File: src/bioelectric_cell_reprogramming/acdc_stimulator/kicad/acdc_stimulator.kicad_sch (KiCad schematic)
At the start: 32 parts, among them IC1 LTC3896EFE#PBF, J1 USB_C_Receptacle_USB2.0_14P, J2 Conn_01x02_Socket, J3 Conn_ARM_SWD_TagConnect_TC203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, SW1 SW_Push, SW2 SW_SPDT, U1 STM32G431CBU3, U2 USBLC6-2SC6, U3 AMS1117-3.3, Y1 16Mhz

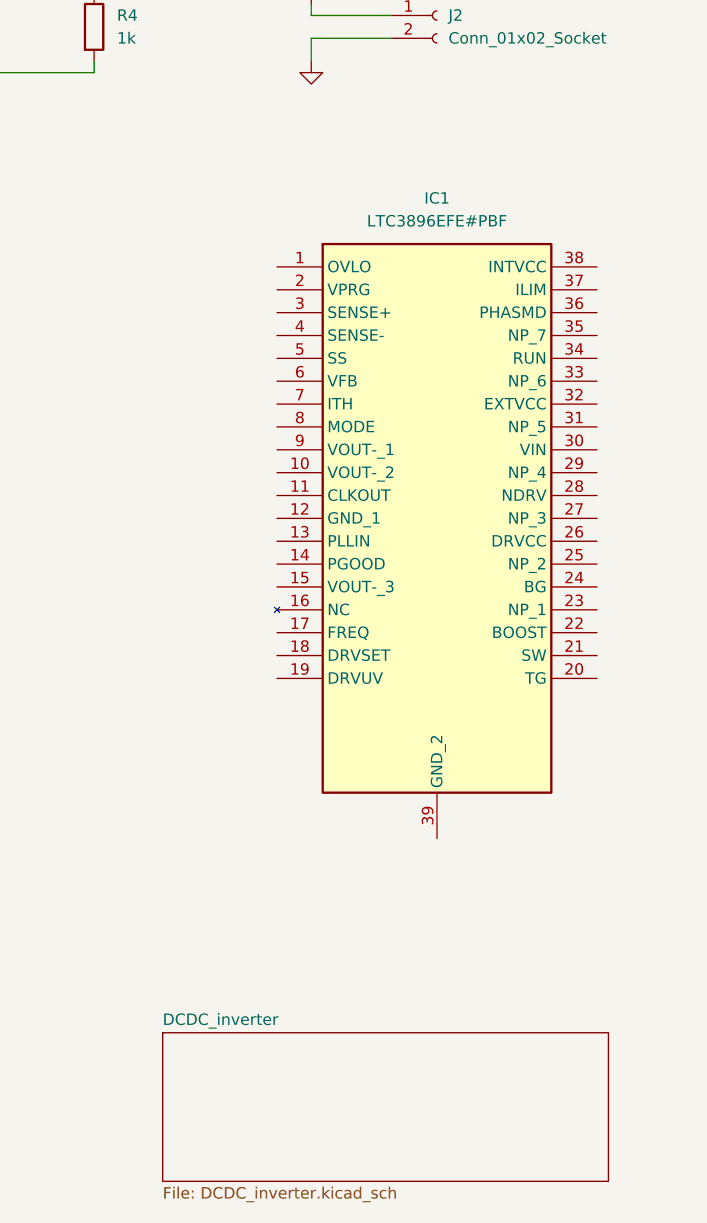
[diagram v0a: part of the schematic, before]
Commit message: finished schematic for DC/DC inverter
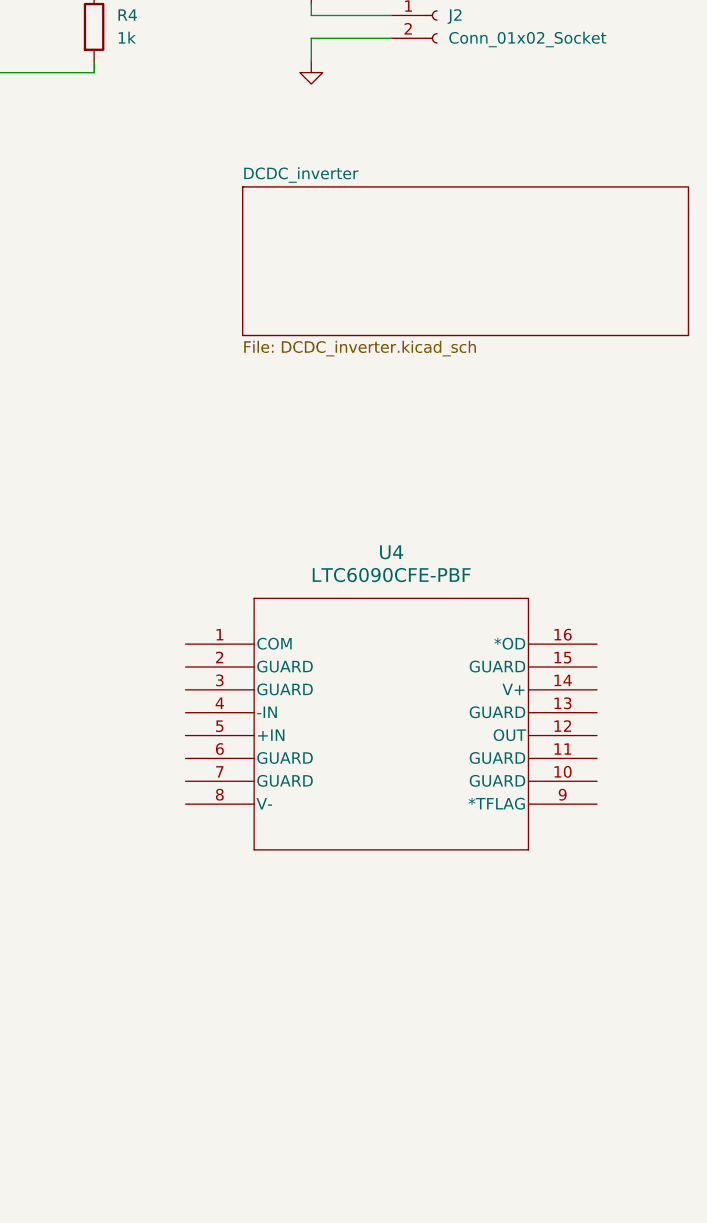
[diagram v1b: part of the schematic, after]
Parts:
- removed IC1: LTC3896EFE#PBF, SOP50P640X120-39N, symbol LTC3896EFE#PBF:LTC3896EFE#PBF
- added U4: LTC6090CFE-PBF, TSSOP-16_FE/BA_LIT, symbol LTC6090CFE_PBF:LTC6090CFE-PBF
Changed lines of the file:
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@@
-	)
-	(symbol
-		(lib_id "LTC3896EFE#PBF:LTC3896EFE#PBF")
-		(at 228.6 55.88 0)
-		(unit 1)
-		(exclude_from_sim no)
-		(in_bom yes)
-		(on_board yes)
-		(dnp no)
-		(fields_autoplaced yes)
-		(property "Reference" "IC1"
-			(at 246.38 48.26 0)
-			(effects
-				(font
-					(size 1.27 1.27)
-				)
-			)
-		)
-		(property "Value" "LTC3896EFE#PBF"
-			(at 246.38 50.8 0)
-			(effects
-				(font
-					(size 1.27 1.27)
-				)
-			)
-		)
-		(property "Footprint" "SOP50P640X120-39N"
-			(at 260.35 150.8 0)
-			(effects
-				(font
-					(size 1.27 1.27)
-				)
-				(justify left top)
-				(hide yes)
-			)
-		)
-		(property "Datasheet" "https://www.analog.com/media/en/technical-documentation/data-sheets/3896f.pdf"
-			(at 260.35 250.8 0)
-			(effects
-				(font
-					(size 1.27 1.27)
-				)
-				(justify left top)
-				(hide yes)
-			)
-		)
-		(property "Description" "LINEAR TECHNOLOGY - LTC3896EFE#PBF - DC/DC CTRL, INVERTING, 900KHZ, TSSOP-38"
-			(at 228.6 55.88 0)
-			(effects
-				(font
-					(size 1.27 1.27)
-				)
-				(hide yes)
-			)
-		)
-		(property "Height" "1.2"
-			(at 260.35 450.8 0)
-			(effects
-				(font
-					(size 1.27 1.27)
-				)
-				(justify left top)
-				(hide yes)
-			)
-		)
-		(property "Manufacturer_Name" "Analog Devices"
-			(at 260.35 550.8 0)
-			(effects
-				(font
-					(size 1.27 1.27)
-				)
-				(justify left top)
-				(hide yes)
-			)
-		)
-		(property "Manufacturer_Part_Number" "LTC3896EFE#PBF"
-			(at 260.35 650.8 0)
-			(effects
-				(font
-					(size 1.27 1.27)
-				)
-				(justify left top)
-				(hide yes)
-			)
-		)
-		(property "Mouser Part Number" "584-LTC3896EFE#PBF"
-			(at 260.35 750.8 0)
-			(effects
-				(font
-					(size 1.27 1.27)
-				)
-				(justify left top)
-				(hide yes)
-			)
-		)
-		(property "Mouser Price/Stock" "https://www.mouser.co.uk/ProductDetail/Analog-Devices/LTC3896EFEPBF?qs=oahfZPh6IAIYB3Kp6X%252BPyQ%3D%3D"
-			(at 260.35 850.8 0)
-			(effects
-				(font
-					(size 1.27 1.27)
-				)
-				(justify left top)
-				(hide yes)
-			)
-		)
-		(property "Arrow Part Number" "LTC3896EFE#PBF"
-			(at 260.35 950.8 0)
-			(effects
-				(font
-					(size 1.27 1.27)
-				)
-				(justify left top)
-				(hide yes)
-			)
-		)
-		(property "Arrow Price/Stock" "https://www.arrow.com/en/products/ltc3896efepbf/analog-devices?region=nac"
-			(at 260.35 1050.8 0)
-			(effects
-				(font
-					(size 1.27 1.27)
-				)
-				(justify left top)
-				(hide yes)
-			)
-		)
-		(pin "38"
-		)
-		(pin "11"
-		)
-		(pin "6"
-		)
-		(pin "8"
-		)
-		(pin "14"
-		)
-		(pin "37"
-		)
-		(pin "9"
-		)
-		(pin "35"
-		)
-		(pin "34"
-		)
-		(pin "22"
-		)
-		(pin "23"
-		)
-		(pin "24"
-		)
-		(pin "21"
-		)
-		(pin "15"
-		)
-		(pin "31"
-		)
-		(pin "27"
-		)
-		(pin "30"
-		)
-		(pin "10"
-		)
-		(pin "39"
-		)
-		(pin "29"
-		)
-		(pin "18"
-		)
-		(pin "3"
-		)
-		(pin "36"
-		)
-		(pin "25"
-		)
-		(pin "26"
-		)
-		(pin "1"
-		)
-		(pin "33"
-		)
-		(pin "17"
-		)
-		(pin "32"
-		)
-		(pin "16"
-		)
-		(pin "4"
-		)
-		(pin "13"
-		)
-		(pin "20"
-		)
-		(pin "5"
-		)
-		(pin "12"
-		)
-		(pin "28"
-		)
-		(pin "7"
-		)
-		(pin "2"
-		)
-		(pin "19"
-		)
-		(instances
-			(project ""
-				(path "/ec70e9f6-566f-44ea-8141-5580f51beca4"
-					(reference "IC1")
-					(unit 1)
-				)
-			)
-		)
 	)
 	(symbol
@@
 	)
 	(symbol
+		(lib_id "LTC6090CFE_PBF:LTC6090CFE-PBF")
+		(at 218.44 97.79 0)
+		(unit 1)
+		(exclude_from_sim no)
+		(in_bom yes)
+		(on_board yes)
+		(dnp no)
+		(fields_autoplaced yes)
+		(property "Reference" "U4"
+			(at 241.3 87.63 0)
+			(effects
+				(font
+					(size 1.524 1.524)
+				)
+			)
+		)
+		(property "Value" "LTC6090CFE-PBF"
+			(at 241.3 90.17 0)
+			(effects
+				(font
+					(size 1.524 1.524)
+				)
+			)
+		)
+		(property "Footprint" "TSSOP-16_FE/BA_LIT"
+			(at 218.44 97.79 0)
+			(effects
+				(font
+					(size 1.27 1.27)
+					(italic yes)
+				)
+				(hide yes)
+			)
+		)
+		(property "Datasheet" "LTC6090CFE-PBF"
+			(at 218.44 97.79 0)
+			(effects
+				(font
+					(size 1.27 1.27)
+					(italic yes)
+				)
+				(hide yes)
+			)
+		)
+		(property "Description" ""
+			(at 218.44 97.79 0)
+			(effects
+				(font
+					(size 1.27 1.27)
+				)
+				(hide yes)
+			)
+		)
+		(pin "15"
+		)
+		(pin "12"
+		)
+		(pin "2"
+		)
+		(pin "9"
+		)
+		(pin "11"
+		)
+		(pin "8"
+		)
+		(pin "16"
+		)
+		(pin "4"
+		)
+		(pin "3"
+		)
+		(pin "6"
+		)
+		(pin "5"
+		)
+		(pin "14"
+		)
+		(pin "13"
+		)
+		(pin "1"
+		)
+		(pin "10"
+		)
+		(pin "7"
+		)
+		(instances
+			(project ""
+				(path "/ec70e9f6-566f-44ea-8141-5580f51beca4"
+					(reference "U4")
+					(unit 1)
+				)
+			)
+		)
+	)
+	(symbol
 		(lib_id "Device:C")
 		(at 86.36 29.21 0)
@@
 	)
 	(sheet
-		(at 215.9 140.97)
+		(at 224.79 46.99)
 		(size 49.53 16.51)
 		(fields_autoplaced yes)
@@
 		)
 		(property "Sheetname" "DCDC_inverter"
-			(at 215.9 140.2584 0)
+			(at 224.79 46.2784 0)
 			(effects
 				(font
@@
 		)
 		(property "Sheetfile" "DCDC_inverter.kicad_sch"
-			(at 215.9 158.0646 0)
+			(at 224.79 64.0846 0)
 			(effects
 				(font
@@
 		)
 		(instances
-			(project "AC_EF"
+			(project "acdc_stimulator"
 				(path "/ec70e9f6-566f-44ea-8141-5580f51beca4"
 					(page "2")

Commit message: ci: main AC/DC schematic done minus incubator peripherals
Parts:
- removed U4: LTC6090CFE-PBF, TSSOP-16_FE/BA_LIT, symbol LTC6090CFE_PBF:LTC6090CFE-PBF
- added C37: 10n, symbol Device:C
- added C38, C40: 100n, symbol Device:C
- added C39: 10uF, symbol Device:C_Polarized
- added C41: 0.1u, symbol Device:C
- added C42: 10u, symbol Device:C
- added C43: 0, symbol Device:C
- added IC1: AD9833BRM-REEL7, SOP50P490X110-10N, symbol AD9833BRM-REEL7:AD9833BRM-REEL7
- added IC3: AD5122BCPZ10-RL7, QFN50P300X300X80-17N-D, symbol AD5122BCPZ10-RL7:AD5122BCPZ10-RL7
- added J4: Screw_Terminal_01x02, symbol Connector:Screw_Terminal_01x02
- added L2, L3: 0, symbol Device:L
- added Q10: BSZ096N10LS5ATMA1, BSZ060NE2LS, symbol BSZ096N10LS5ATMA1:BSZ096N10LS5ATMA1
- added R11, R18, R19: 10k, symbol Device:R
- added R12: 172k, symbol Device:R
- added R15, R16, R17: 0, symbol Device:R
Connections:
- net +3.3V: now also C41.1, C42.1, IC3.9 (VDD)
- net +5V: now also C37.1, C38.2, C39.1, IC1.2 (VDD)
- net GND: now also C38.1, C39.2, C40.1, C41.2, C42.2, IC1.4 (DGND), IC1.9 (AGND), IC3.1 (GND), IC3.17 (EP), IC3.4 (B1), IC3.5 (VSS), R11.1, R19.2
- net HSE_OUT: now also IC1.5 (MCLK)
- net DAC_DC: now reaches U1.12 (PA4)
- net DAC_AC: now reaches U1.13 (PA5)
- net DAC_AC: now also R18.1
- net H_Bridge_IN1: now reaches U1.25 (PB12)
- net H_Bridge_IN1: now also R15.1
- net H_Bridge_IN2: now reaches U1.26 (PB13)
- net H_Bridge_IN2: now also R16.1
- net VAC_ON: now reaches U1.29 (PC6)
- net VAC_ON: now also Q10.4 (G)
- net FG_CS: now reaches U1.30 (PA8)
- net FG_CS: now also IC1.8 (FSYNC)
- net POT_CS: now reaches U1.31 (PA9)
- net POT_CS: now also IC3.14 (~{SYNC})
- net SCLK: now reaches U1.39 (PC10)
- net SCLK: now also IC1.7 (SCLK), IC3.11 (SCLK)
- net SDI: now reaches U1.40 (PC11)
- net SDI: now also IC3.12 (SDI)
- net SDO: now reaches U1.43 (PB5)
- net SDO: now also IC1.6 (SDATA), IC3.13 (SDO)
- new net: IC3.10 (VLOGIC), IC3.16 (~{RESET})
- new net: C37.2, IC1.1 (COMP)
- new net: C40.2, IC1.3 (CAP/2.5V)
- new net: J4.1 (Pin_1), L2.2
- new net: C43.1, J4.2 (Pin_2), L3.2
- new net FG_OUT: IC1.10 (VOUT), IC3.2 (A1)
- new net H_Bridge/IN1: R15.2
- new net H_Bridge/IN2: R16.2
- new net LTC6090_AC/+IN: R18.2, R19.1
- new net LTC6090_AC/OUT: Q10.5 (D_1), Q10.6 (D_2), Q10.7 (D_3), Q10.8 (D_4), R17.2
- new net LTC6090_DC/-IN: R11.2, R12.1
- new net POT_OUT: IC3.3 (W1), R17.1
- new net VAC: C43.2, Q10.1 (S_1), Q10.2 (S_2), Q10.3 (S_3)
- new net VDC1: L2.1
- new net VDC2: L3.1
- new net V_DC: R12.2
- no-connect marks 0 -> 4
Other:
- added sheet H_Bridge (H_Bridge.kicad_sch)
- added sheet LTC6090_AC (LTC6090_AC.kicad_sch)
- added sheet LTC6090_DC (LTC6090_DC.kicad_sch)
- moved on the sheet: J2

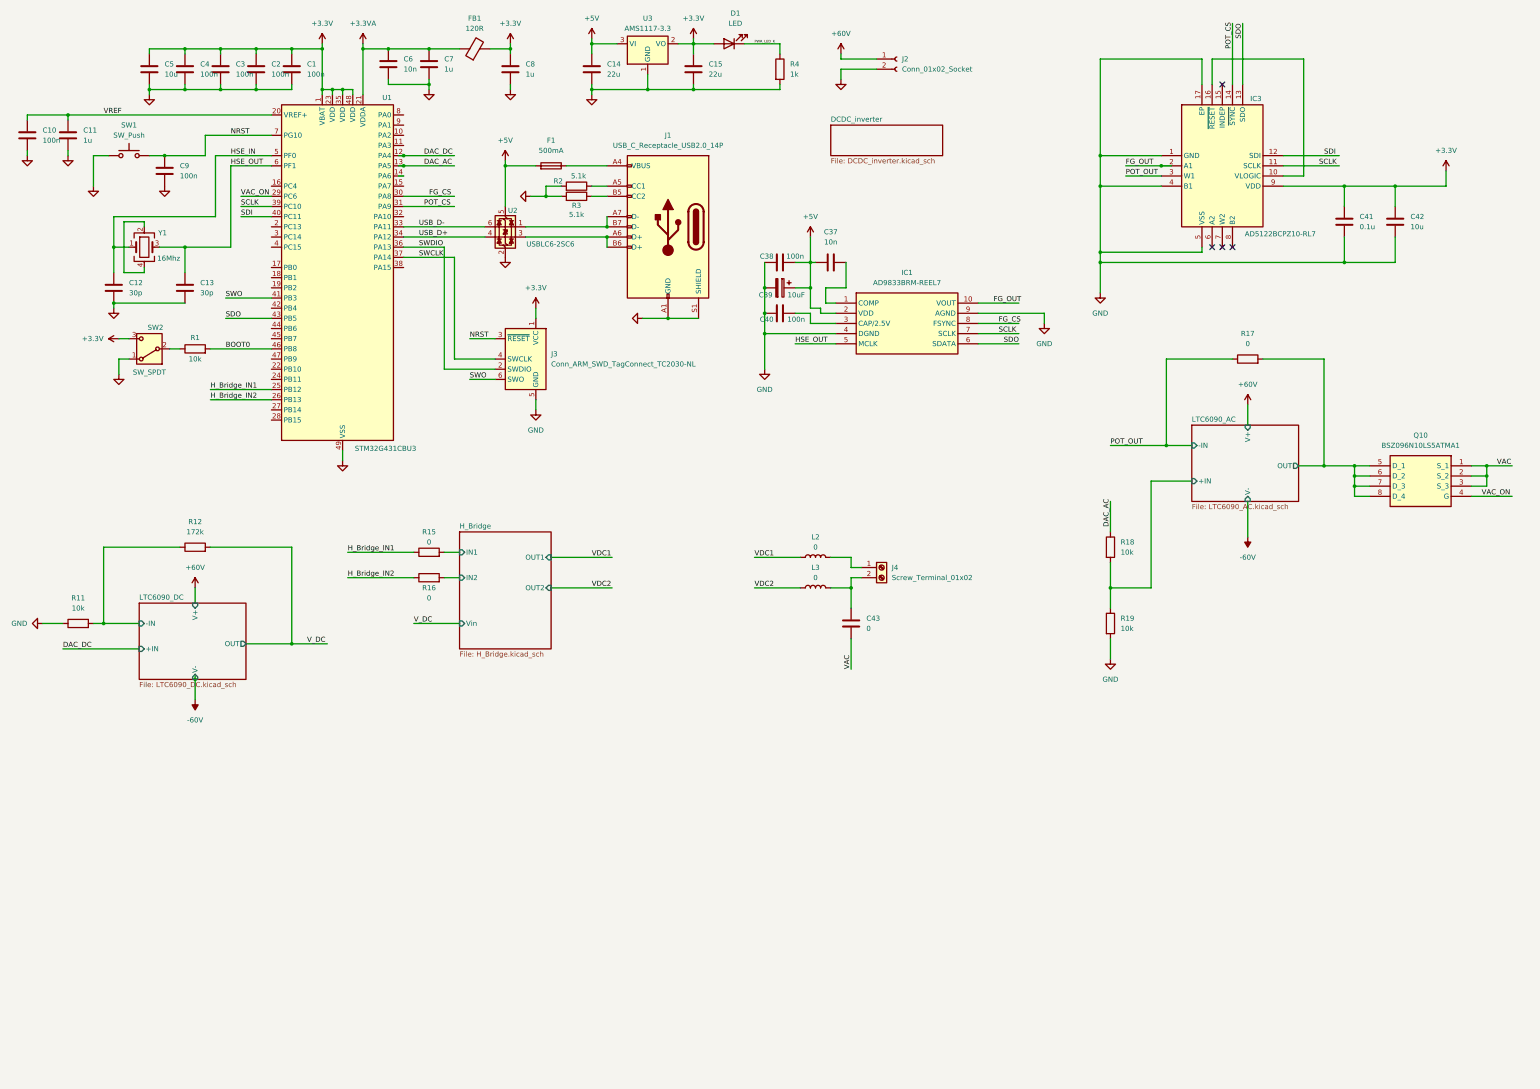
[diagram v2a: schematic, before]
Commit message: fix: added new STM32 with 3 DAC output pins
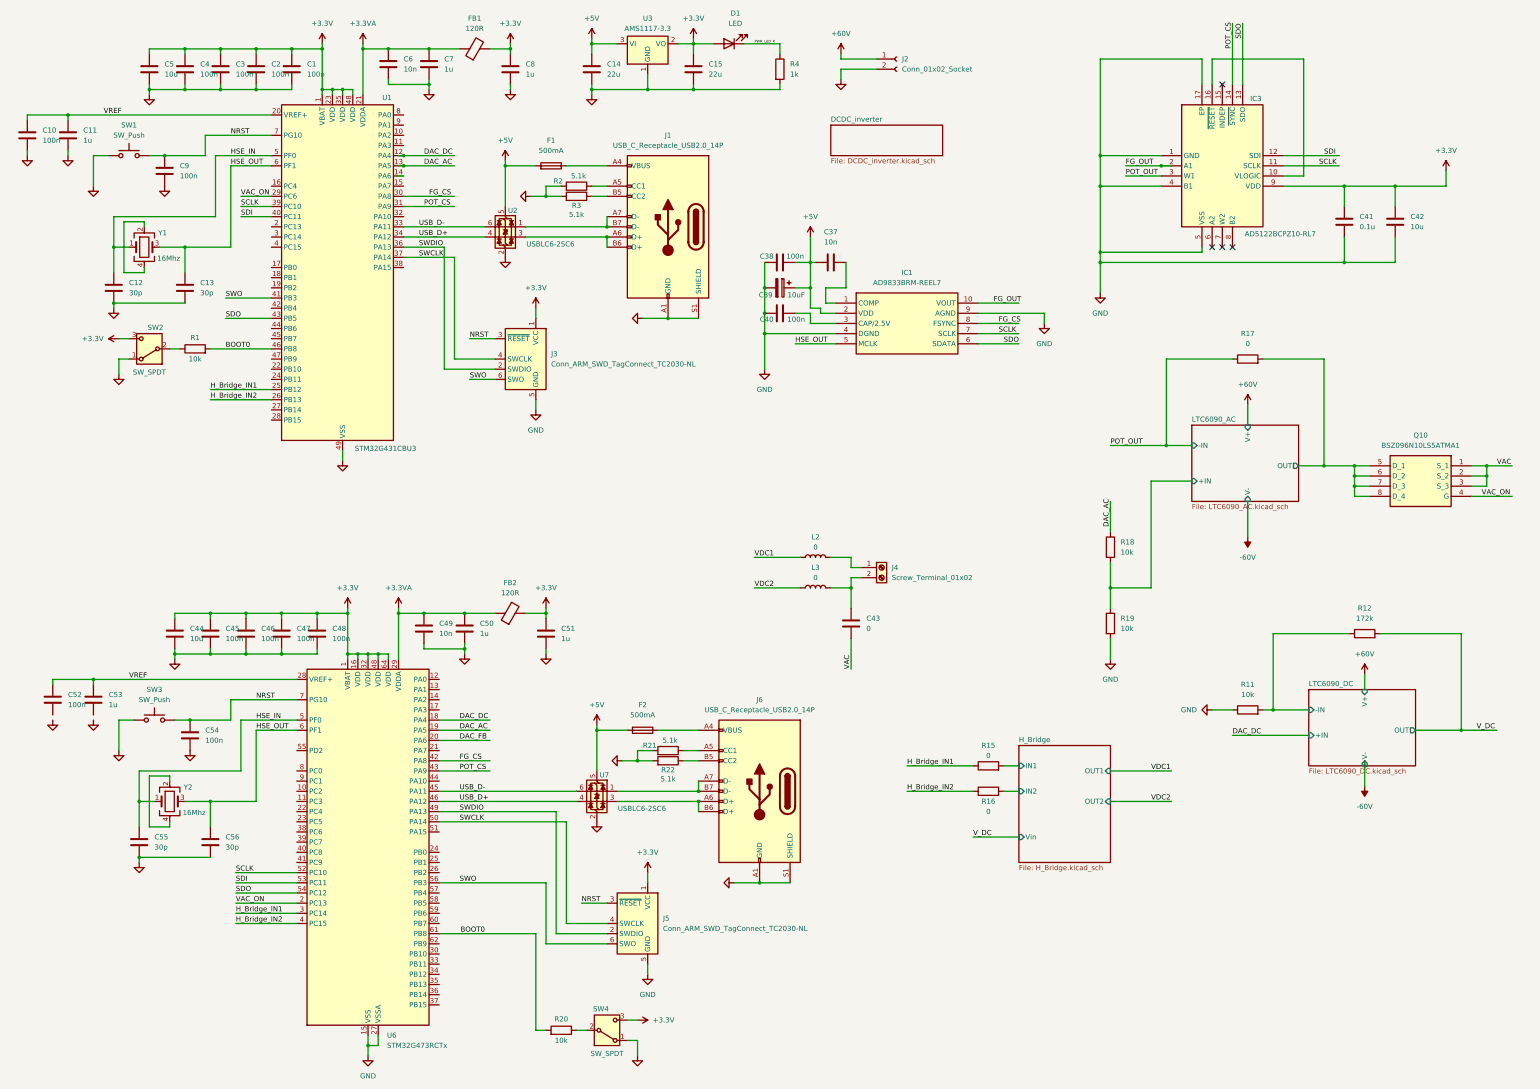
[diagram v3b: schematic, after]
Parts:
- added C44: 10u, symbol Device:C
- added C45, C46, C47, C48: 100n, symbol Device:C
- added C49: 10n, symbol Device:C
- added C50, C51: 1u, symbol Device:C
- added C52, C54: 100n, Capacitor_SMD:C_0402_1005Metric, symbol Device:C
- added C53: 1u, Capacitor_SMD:C_0402_1005Metric, symbol Device:C
- added C55, C56: 30p, symbol Device:C
- added F2: 500mA, Fuse:Fuse_0603_1608Metric, symbol Device:Fuse
- added FB2: 120R, symbol Device:FerriteBead
- added J5: Conn_ARM_SWD_TagConnect_TC2030-NL, Connector:Tag-Connect_TC2030-IDC-NL_2x03_P1.27mm_Vertical, symbol Connector:Conn_ARM_SWD_TagConnect_TC2030-NL
- added J6: USB_C_Receptacle_USB2.0_14P, Connector_USB:USB_C_Receptacle_GCT_USB4105-xx-A_16P_TopMnt_Horizontal, symbol Connector:USB_C_Receptacle_USB2.0_14P
- added R20: 10k, symbol Device:R
- added R21, R22: 5.1k, Resistor_SMD:R_0603_1608Metric, symbol Device:R
- added SW3: SW_Push, Button_Switch_THT:SW_PUSH-12mm_Wuerth-430476085716, symbol Switch:SW_Push
- added SW4: SW_SPDT, symbol Switch:SW_SPDT
- added U6: STM32G473RCTx, Package_QFP:LQFP-64_10x10mm_P0.5mm, symbol MCU_ST_STM32G4:STM32G473RCTx
- added U7: USBLC6-2SC6, Package_TO_SOT_SMD:SOT-23-6, symbol Power_Protection:USBLC6-2SC6
- added Y2: 16Mhz, symbol Device:Crystal_GND24
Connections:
- net +3.3V: now also C44.1, C45.1, C46.1, C47.1, C48.1, C51.1, FB2.2, J5.1 (VCC), SW4.3 (C), U6.1 (VBAT), U6.16 (VDD), U6.32 (VDD), U6.48 (VDD), U6.64 (VDD)
- net +3.3VA: now also C49.1, C50.1, FB2.1, U6.29 (VDDA)
- net +5V: now also F2.2, U7.5 (VBUS)
- net BOOT0: now also R20.2, U6.61 (PB8)
- net DAC_AC: now also U6.19 (PA5)
- net DAC_DC: now also U6.18 (PA4)
- net FG_CS: now also U6.42 (PA8)
- net GND: now also C44.2, C45.2, C46.2, C47.2, C48.2, C49.2, C50.2, C51.2, C54.2, C55.2, C56.2, J5.5 (GND), J6.A1 (GND), J6.A12 (GND), J6.B1 (GND), J6.B12 (GND), J6.S1 (SHIELD), R21.2, R22.2, SW3.1, SW4.1 (A), U6.15 (VSS), U6.27 (VSSA), U6.31 (VSS), U6.47 (VSS), U6.63 (VSS), U7.2 (GND)
- net HSE_IN: now also C55.1, U6.5 (PF0), Y2.1
- net HSE_OUT: now also C56.1, U6.6 (PF1), Y2.3
- net H_Bridge_IN1: now also U6.3 (PC14)
- net H_Bridge_IN2: now also U6.4 (PC15)
- net NRST: now also C54.1, J5.3 (~{RESET}), SW3.2, U6.7 (PG10)
- net POT_CS: now also U6.43 (PA9)
- net SCLK: now also U6.52 (PC10)
- net SDI: now also U6.53 (PC11)
- net SDO: now also U6.54 (PC12)
- net SWCLK: now also J5.4 (SWCLK), U6.50 (PA14)
- net SWDIO: now also J5.2 (SWDIO), U6.49 (PA13)
- net SWO: now also J5.6 (SWO), U6.56 (PB3)
- net USB_D+: now also U6.46 (PA12), U7.4 (I/O2)
- net USB_D-: now also U6.45 (PA11), U7.6 (I/O1)
- net VAC_ON: now also U6.2 (PC13)
- net VREF: now also C52.1, C53.1, U6.28 (VREF+)
- new net: F2.1, J6.A4 (VBUS), J6.A9 (VBUS), J6.B4 (VBUS), J6.B9 (VBUS)
- new net: J6.A5 (CC1), R21.1
- new net: J6.A6 (D+), J6.B6 (D+), U7.3 (I/O2)
- new net: J6.A7 (D-), J6.B7 (D-), U7.1 (I/O1)
- new net: J6.B5 (CC2), R22.1
- new net: R20.1, SW4.2 (B)
- new net: Y2.2, Y2.4
- new net DAC_FB: U6.20 (PA6)
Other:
- moved on the sheet: R11, R12, R15, R16
